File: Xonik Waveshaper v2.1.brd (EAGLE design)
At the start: 63.5 x 29.1 mm, 86 parts, among them IC1 TL074D, IC2 TL074D, IC3 TL074D, IC4 TL072D, IC5 4013D, T1 2n3904

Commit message: Changed to R0603 and 3v3 operation
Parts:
- added 1, 2: 390R, rcl:R0603
- 10, 11, 12, 13, 14, 15, 16, 17, 18, 19, 20, 23, 24, 25, 28, 29, 3, 30, 35, 36, 37, 38, 39, 4, 40, 41, 44, 45, 46, 47, 48, 49, 5, 50, 6, 7, 8: device resistor:R0805 -> rcl:R0603
- 26, 27: value 10k -> 6k2; device resistor:R0805 -> rcl:R0603
- C1, C2, C3, C4, C5, C6, C7, C8: device resistor:C0805 -> rcl:C0603
- C10, C11, C16: device resistor:C0603K -> rcl:C0603
- moved 26 2.25 mm to (59.4, 27.0)
- moved 27 1.04 mm to (56.7, 10.2), turned to 180 degrees
- moved C5 0.63 mm to (62.2, 24.8)
- moved C6 0.63 mm to (59.7, 9.21)
- moved C8 0.63 mm to (62.2, 9.21)
- renumbered +5V to +3V3
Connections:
- net +5V renamed +3V3
- new net N$25: 2.2, 27.1
- new net N$8: 1.2, 26.1
- net N$32: now also 1.1; no longer 26.1
- net N$35: now also 2.1; no longer 27.1
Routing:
- net N$25: track 0.00 -> 3.67 mm
- net N$30: track 20.5 -> 24.1 mm
- net N$26: track 25.9 -> 29.4 mm
- net N$23: track 15.3 -> 17.9 mm
- net N$29: track 23.2 -> 20.8 mm
- net N$19: track 19.2 -> 21.6 mm
- net N$17: track 49.4 -> 47.1 mm
- net N$34: track 15.4 -> 17.5 mm
- net N$9: track 51.9 -> 50.2 mm
- net N$8: track 0.00 -> 1.47 mm
- net N$18: track 31.1 -> 30.1 mm
- net N$39: track 13.8 -> 14.7 mm
- net N$6: track 13.6 -> 12.8 mm
- net N$14: track 32.4 -> 31.7 mm
- net N$22: track 16.9 -> 16.3 mm
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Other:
- board text added: "+3V3"
- board text removed: "+5V"

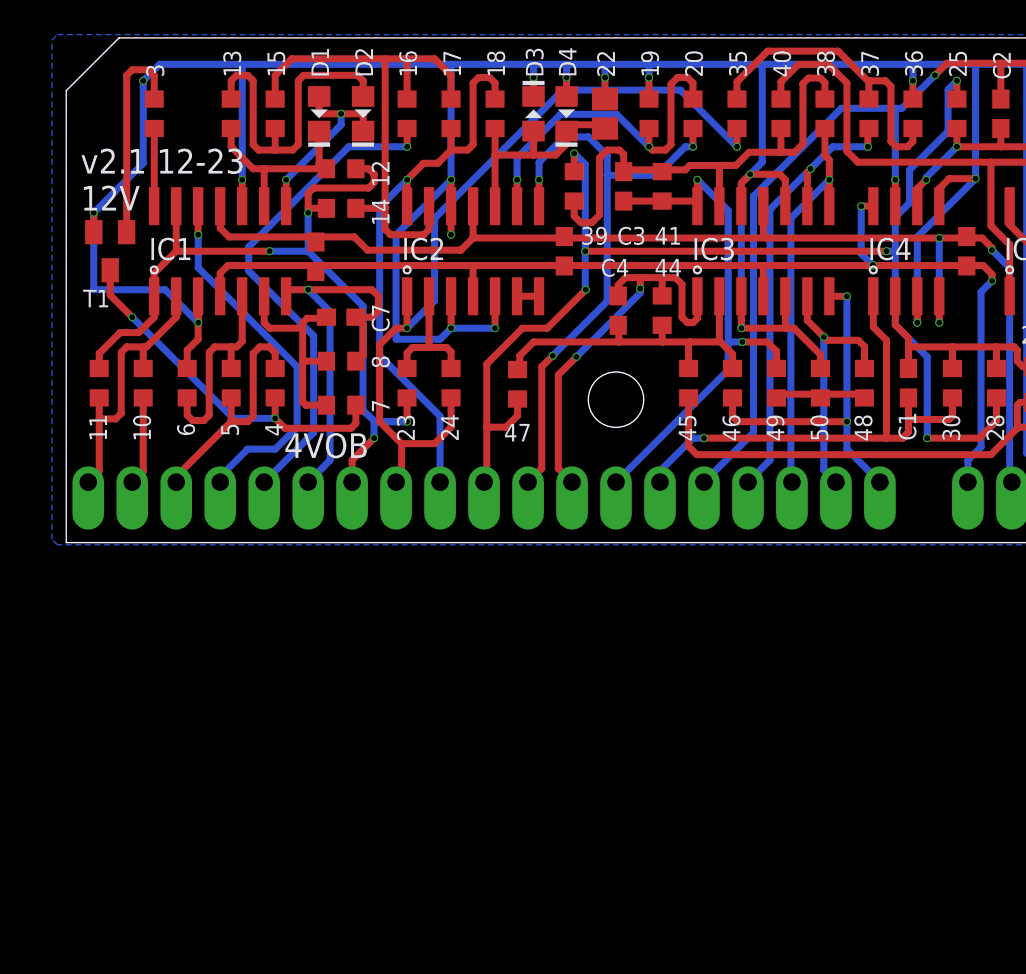
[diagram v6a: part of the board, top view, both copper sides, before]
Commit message: Updated component values after simulation
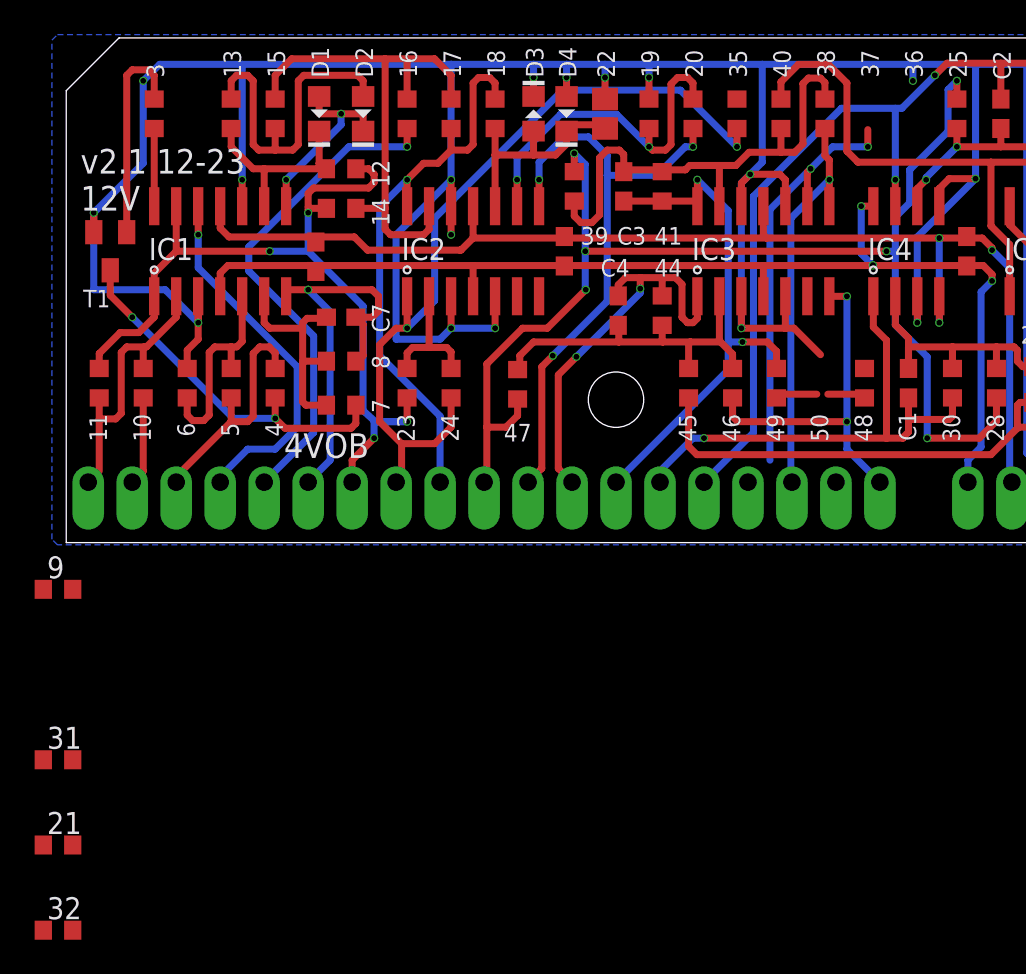
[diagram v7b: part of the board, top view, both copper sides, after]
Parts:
- removed 36, 37, 50: 27k, rcl:R0603
- added 21: 15k, rcl:R0603
- added 31: 27k, rcl:R0603
- added 32: 33k, rcl:R0603
- added 9: 30k, rcl:R0603
- 16: value 150k -> 100k
- 35, 49: value 27k -> 100k
- 38, 39, 41, 44, 46, 47: value 47k -> 49.9k
- 40, 45: value 47k -> 33k
- 48: value 27k -> 33k
- 5, 8: value 20k -> 200k
- 6, 7: value 10k -> 100k
- C7: value 6pF -> 3pF
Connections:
- new net N$38: 21.1, CENTER.1
- new net N$42: 31.1, 9.2, IC2.7
- net GND: no longer 36.1, 50.2
- net N$1: now also 21.2, 9.1; no longer IC2.7
- net N$10: now also 31.2; no longer CENTER.1
- net N$21: now also IC3.6; no longer 50.1
- net N$23: now also 32.2, ST1.1; no longer 35.2, 36.2, 37.2
- net N$24: now also 32.1, 35.2; no longer 37.1, ST1.1
- net N$28: no longer IC3.6
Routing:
- net N$23: track 17.9 -> 0.00 mm
- net N$28: track 15.3 -> 0.00 mm, vias 1 -> 0
- net N$24: track 26.7 -> 24.9 mm
- net GND: track 257.8 -> 255.9 mm
- net N$1: track 1.27 -> 0.00 mm
- net N$10: track 16.6 -> 15.7 mm
- net N$21: track 5.65 -> 4.87 mm

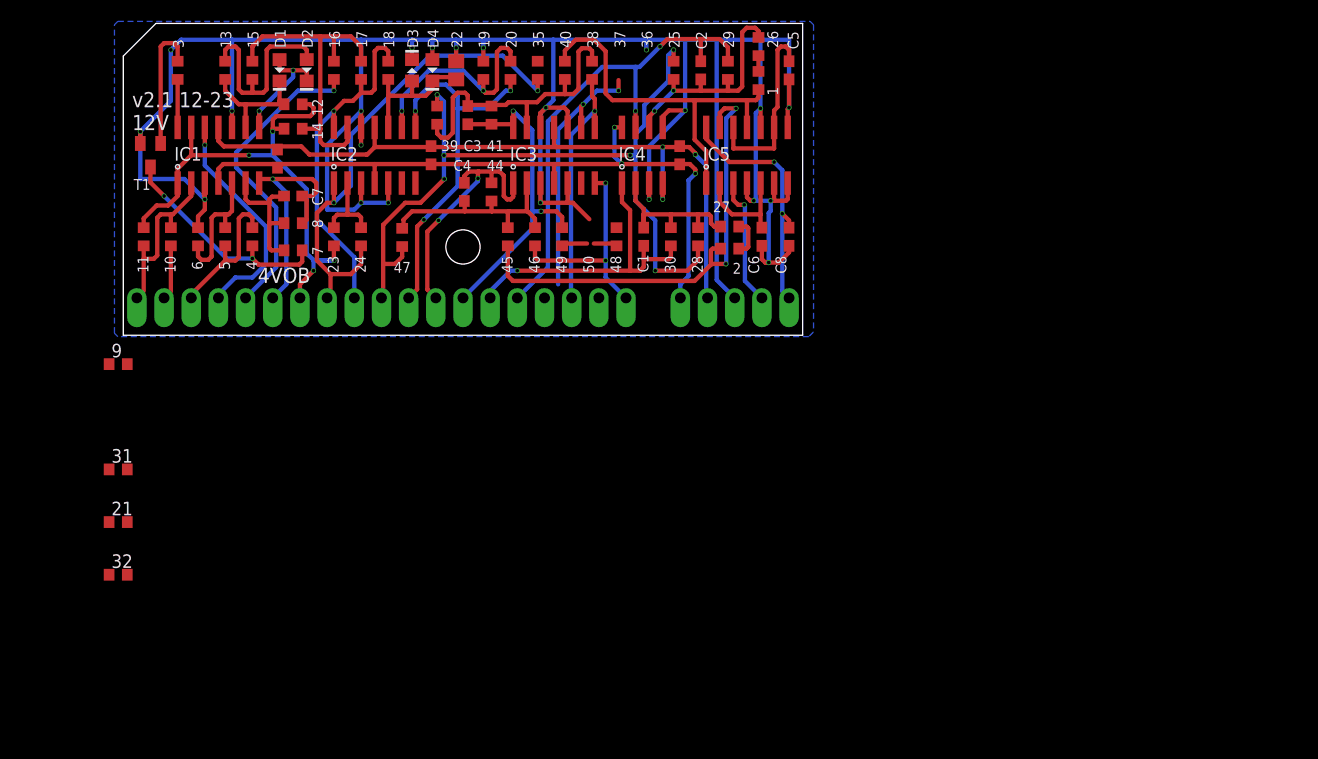
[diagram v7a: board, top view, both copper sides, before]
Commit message: Changed size and number of decoupling caps
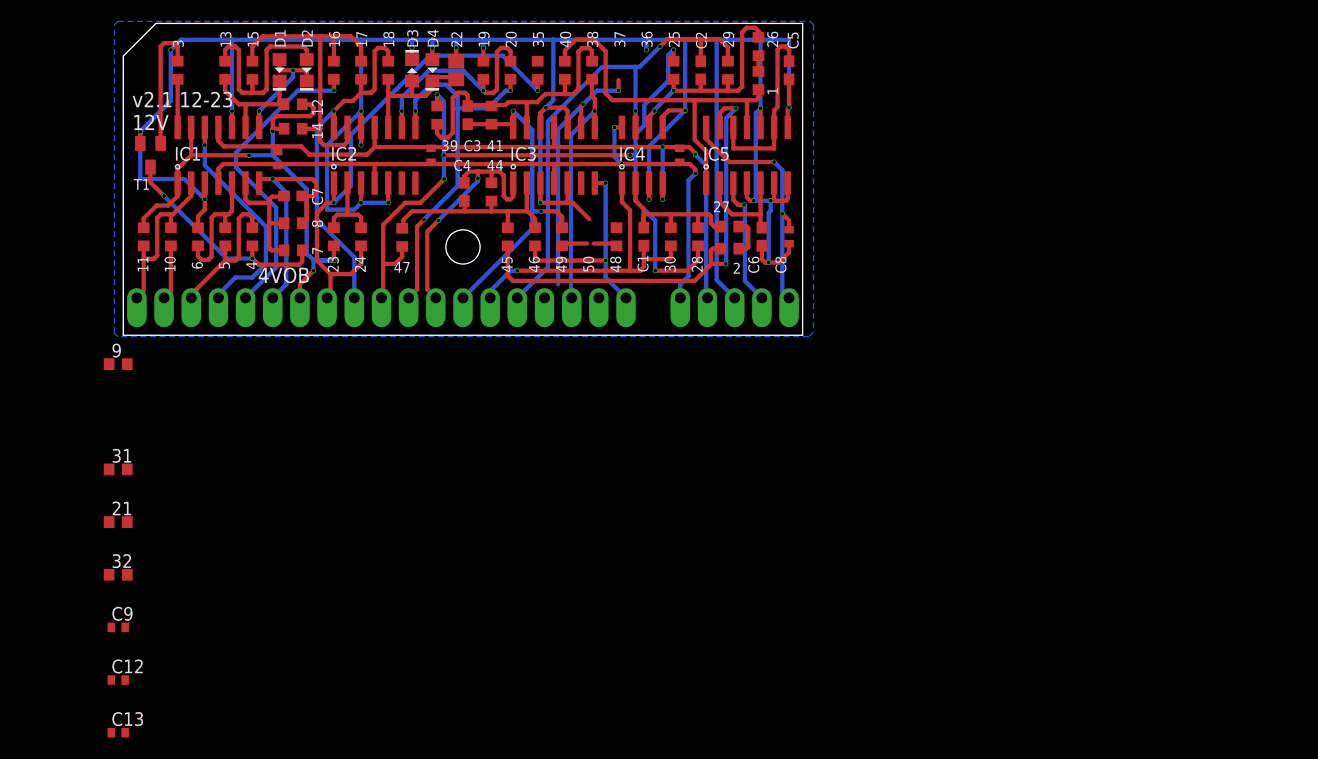
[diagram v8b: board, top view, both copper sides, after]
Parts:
- added C12, C13, C9: 1uF, rcl:C0402
- C10, C11, C16, C8: value 100nF -> 1uF; device rcl:C0603 -> rcl:C0402
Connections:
- net -12V: now also C12.1, C13.1, C9.1; no longer C10.1, C11.1, C16.1
- net GND: now also C10.1, C11.1, C12.2, C13.2, C16.1, C9.2
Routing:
- net -12V: track 71.6 -> 70.8 mm
